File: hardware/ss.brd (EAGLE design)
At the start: 65 x 56 mm, 86 parts, among them IC1 DS3231, Q1 BSS138, Q3 si2305cd, Q4 si2305cd, Q5 8MHz, Q6 si2305cd, T1 BC846, T2 BC846, U1 SPX5205 3v3, U17 AVR_SPI_PRG_6PTH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

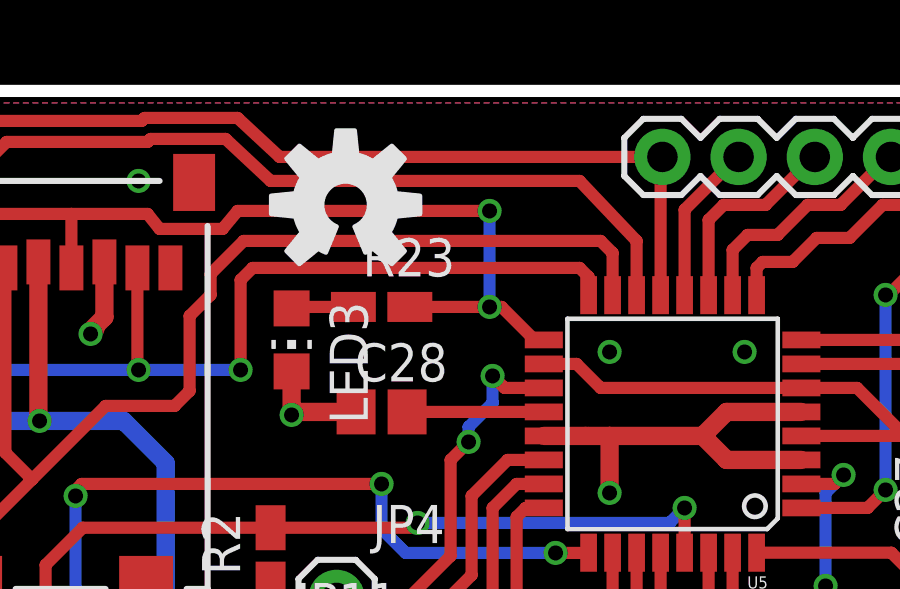
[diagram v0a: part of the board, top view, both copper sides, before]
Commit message: d9 needs external weak pullup during programming
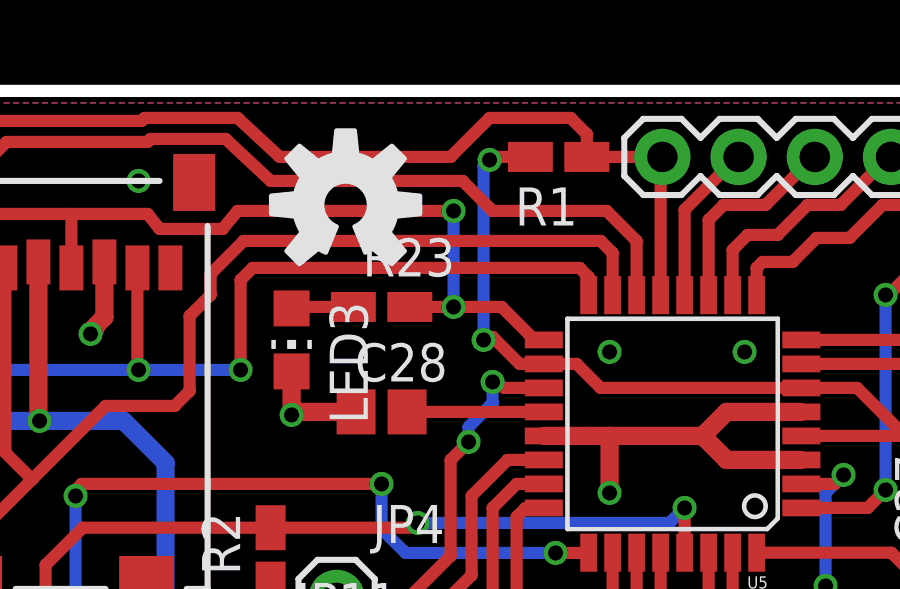
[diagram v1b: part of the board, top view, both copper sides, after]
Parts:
- added R1: 100K, rcl:R0805W
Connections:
- net +3V3: now also R1.2
- net D9: now also R1.1
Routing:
- net +3V3: track 173.7 -> 183.6 mm, vias 9 -> 11
- net D9: track 46.5 -> 48.0 mm
- net SCK: track 48.0 -> 46.8 mm
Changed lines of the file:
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@@
 <element name="R18" library="rcl" package="R0805W" value="100k" x="15.2" y="25.6" rot="R180"/>
 <element name="SJ2" library="jumper" package="SJ" value="J2" x="18.3" y="28.9" rot="R270"/>
+<element name="R1" library="rcl" package="R0805W" value="100K" x="38.1" y="53.8" rot="R180"/>
 </elements>
 <signals>
@@
 <wire x1="55.4" y1="42.7" x2="55.6" y2="42.9" width="0.6096" layer="1"/>
 <wire x1="55.6" y1="42.9" x2="57.9" y2="42.9" width="0.6096" layer="1"/>
+<contactref element="R1" pad="2"/>
+<wire x1="35.6" y1="47.7" x2="35.9" y2="47.8" width="0.4064" layer="1"/>
+<wire x1="35.9" y1="53.8" x2="35.8" y2="53.7" width="0.4064" layer="1"/>
+<wire x1="37.16" y1="53.8" x2="35.9" y2="53.8" width="0.4064" layer="1"/>
+<via x="35.6" y="47.7" extent="1-16" drill="0.5"/>
+<via x="35.8" y="53.7" extent="1-16" drill="0.5"/>
+<wire x1="35.9" y1="47.8" x2="36.8" y2="46.9" width="0.4064" layer="1"/>
+<wire x1="36.8" y1="46.9" x2="37.6074" y2="46.9" width="0.4064" layer="1"/>
+<wire x1="35.8" y1="53.7" x2="35.6" y2="53.5" width="0.4064" layer="16"/>
+<wire x1="35.6" y1="53.5" x2="35.6" y2="47.7" width="0.4064" layer="16"/>
 </signal>
 <signal name="+5V">
@@
 <wire x1="6.6" y1="45.105" x2="6.595" y2="45.1" width="0.4064" layer="1"/>
 <wire x1="37.6074" y1="47.7" x2="37.3" y2="47.7" width="0.4064" layer="1"/>
-<wire x1="35.8" y1="48.8" x2="35.8" y2="52" width="0.4064" layer="16"/>
-<via x="35.8" y="48.8" extent="1-16" drill="0.5"/>
-<via x="35.8" y="52" extent="1-16" drill="0.5"/>
+<wire x1="34.6" y1="48.8" x2="34.6" y2="52" width="0.4064" layer="16"/>
+<via x="34.6" y="48.8" extent="1-16" drill="0.5"/>
+<via x="34.6" y="52" extent="1-16" drill="0.5"/>
 <wire x1="21.86" y1="51.9" x2="21.86" y2="50.1" width="0.4064" layer="1"/>
 <wire x1="21.86" y1="51.9" x2="15.3" y2="51.9" width="0.4064" layer="1"/>
@@
 <wire x1="6.6" y1="45.105" x2="6.6" y2="41.96" width="0.6096" layer="1"/>
 <wire x1="6.6" y1="41.96" x2="6.66" y2="41.9" width="0.6096" layer="1"/>
-<wire x1="33.14" y1="48.8" x2="35.8" y2="48.8" width="0.4064" layer="1"/>
+<wire x1="33.14" y1="48.8" x2="34.6" y2="48.8" width="0.4064" layer="1"/>
 <wire x1="21.86" y1="51.9" x2="24.4" y2="51.9" width="0.4064" layer="1"/>
 <wire x1="24.4" y1="51.9" x2="24.8" y2="51.4" width="0.4064" layer="1"/>
 <wire x1="24.8" y1="51.4" x2="26.9" y2="51.4" width="0.4064" layer="1"/>
 <wire x1="26.9" y1="51.4" x2="27.4" y2="52" width="0.4064" layer="1"/>
-<wire x1="27.4" y1="52" x2="35.8" y2="52" width="0.4064" layer="1"/>
+<wire x1="27.4" y1="52" x2="34.6" y2="52" width="0.4064" layer="1"/>
 <wire x1="37.3" y1="47.7" x2="36.2" y2="48.8" width="0.4064" layer="1"/>
-<wire x1="36.2" y1="48.8" x2="35.8" y2="48.8" width="0.4064" layer="1"/>
+<wire x1="36.2" y1="48.8" x2="34.6" y2="48.8" width="0.4064" layer="1"/>
 </signal>
 <signal name="MISO">
@@
 <contactref element="U5" pad="14"/>
 <wire x1="40.7" y1="49.1926" x2="40.7" y2="51" width="0.4064" layer="1"/>
-<wire x1="40.7" y1="51" x2="38.8" y2="53" width="0.4064" layer="1"/>
-<wire x1="38.8" y1="53" x2="28.5" y2="53" width="0.4064" layer="1"/>
+<wire x1="34.9" y1="53" x2="28.5" y2="53" width="0.4064" layer="1"/>
 <wire x1="18.6" y1="48.2" x2="18.6" y2="48.4" width="0.4064" layer="1"/>
 <wire x1="18.6" y1="53" x2="18.6" y2="48.2" width="0.4064" layer="16"/>
@@
 <wire x1="19.7" y1="54.3" x2="18.6" y2="53.2" width="0.4064" layer="1"/>
 <wire x1="18.6" y1="53.2" x2="18.6" y2="53" width="0.4064" layer="1"/>
+<wire x1="34.9" y1="53" x2="35.9" y2="52" width="0.4064" layer="1"/>
+<wire x1="35.9" y1="52" x2="39.7" y2="52" width="0.4064" layer="1"/>
+<wire x1="39.7" y1="52" x2="40.7" y2="51" width="0.4064" layer="1"/>
 </signal>
 <signal name="N$22">
@@
 <wire x1="41.5" y1="49.1926" x2="41.5" y2="53.8" width="0.4064" layer="1"/>
 <wire x1="41.5" y1="53.8" x2="41.56" y2="53.8" width="0.4064" layer="1"/>
-<wire x1="28.8" y1="53.8" x2="41.56" y2="53.8" width="0.4064" layer="1"/>
 <wire x1="28.8" y1="53.8" x2="27.4" y2="55.1" width="0.4064" layer="1"/>
 <wire x1="27.4" y1="55.1" x2="24.3" y2="55.1" width="0.4064" layer="1"/>
 <wire x1="24.3" y1="55.1" x2="24.2" y2="55" width="0.4064" layer="1"/>
 <wire x1="24.2" y1="55" x2="19.1" y2="55" width="0.4064" layer="1"/>
+<contactref element="R1" pad="1"/>
+<wire x1="39.04" y1="53.8" x2="41.56" y2="53.8" width="0.4064" layer="1"/>
+<wire x1="39.04" y1="53.8" x2="39.04" y2="54.56" width="0.4064" layer="1"/>
+<wire x1="39.04" y1="54.56" x2="38.5" y2="55.1" width="0.4064" layer="1"/>
+<wire x1="38.5" y1="55.1" x2="35.8" y2="55.1" width="0.4064" layer="1"/>
+<wire x1="35.8" y1="55.1" x2="34.5" y2="53.8" width="0.4064" layer="1"/>
+<wire x1="34.5" y1="53.8" x2="28.8" y2="53.8" width="0.4064" layer="1"/>
 </signal>
 <signal name="SDA">
@@
 <contactref element="U5" pad="19"/>
 <via x="35.1" y="44.3" extent="1-16" drill="0.5"/>
-<via x="35.9" y="46.5" extent="1-16" drill="0.5"/>
+<via x="35.9" y="46.3" extent="1-16" drill="0.5"/>
 <wire x1="35.1" y1="44.8" x2="35.1" y2="44.3" width="0.4064" layer="16"/>
 <wire x1="37.6074" y1="46.1" x2="36.3" y2="46.1" width="0.4064" layer="1"/>
 <wire x1="35.1" y1="44.3" x2="34.5" y2="43.7" width="0.4064" layer="1"/>
-<wire x1="36.3" y1="46.1" x2="35.9" y2="46.5" width="0.4064" layer="1"/>
-<wire x1="35.9" y1="46.5" x2="35.9" y2="45.6" width="0.4064" layer="16"/>
+<wire x1="36.3" y1="46.1" x2="35.9" y2="46.3" width="0.4064" layer="1"/>
+<wire x1="35.9" y1="46.3" x2="35.9" y2="45.6" width="0.4064" layer="16"/>
 <wire x1="35.9" y1="45.6" x2="35.1" y2="44.8" width="0.4064" layer="16"/>
 <contactref element="JP4" pad="1"/>

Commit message: thermocouple t- must be grounded
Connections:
- removed net N$30: JP9.2, U$3.2
- net GND: now also JP9.2, U$3.2
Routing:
- net GND: track 114.2 -> 117.7 mm
- net N$30: track 3.49 -> 0.00 mm
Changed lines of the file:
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@@
 <via x="34.7" y="14.6" extent="1-16" drill="0.5"/>
 <wire x1="49.5" y1="28.1999" x2="49.5" y2="26.4" width="0.6096" layer="1"/>
+<contactref element="U$3" pad="2"/>
+<contactref element="JP9" pad="2"/>
+<wire x1="9.135" y1="50.3" x2="9.135" y2="52.595" width="0.6096" layer="1"/>
+<wire x1="9.135" y1="52.595" x2="9.84" y2="53.3" width="0.6096" layer="1"/>
+<wire x1="9.84" y1="53.3" x2="10.04" y2="53.3" width="0.6096" layer="1"/>
 </signal>
 <signal name="VIN">
@@
 <wire x1="7.5" y1="53.335" x2="7.5" y2="53.3" width="0.4064" layer="1"/>
 </signal>
-<signal name="N$30">
-<contactref element="U$3" pad="2"/>
-<contactref element="JP9" pad="2"/>
-<wire x1="9.135" y1="50.3" x2="9.135" y2="52.595" width="0.6096" layer="1"/>
-<wire x1="9.135" y1="52.595" x2="9.84" y2="53.3" width="0.6096" layer="1"/>
-<wire x1="9.84" y1="53.3" x2="10.04" y2="53.3" width="0.6096" layer="1"/>
-</signal>
 <signal name="A6">

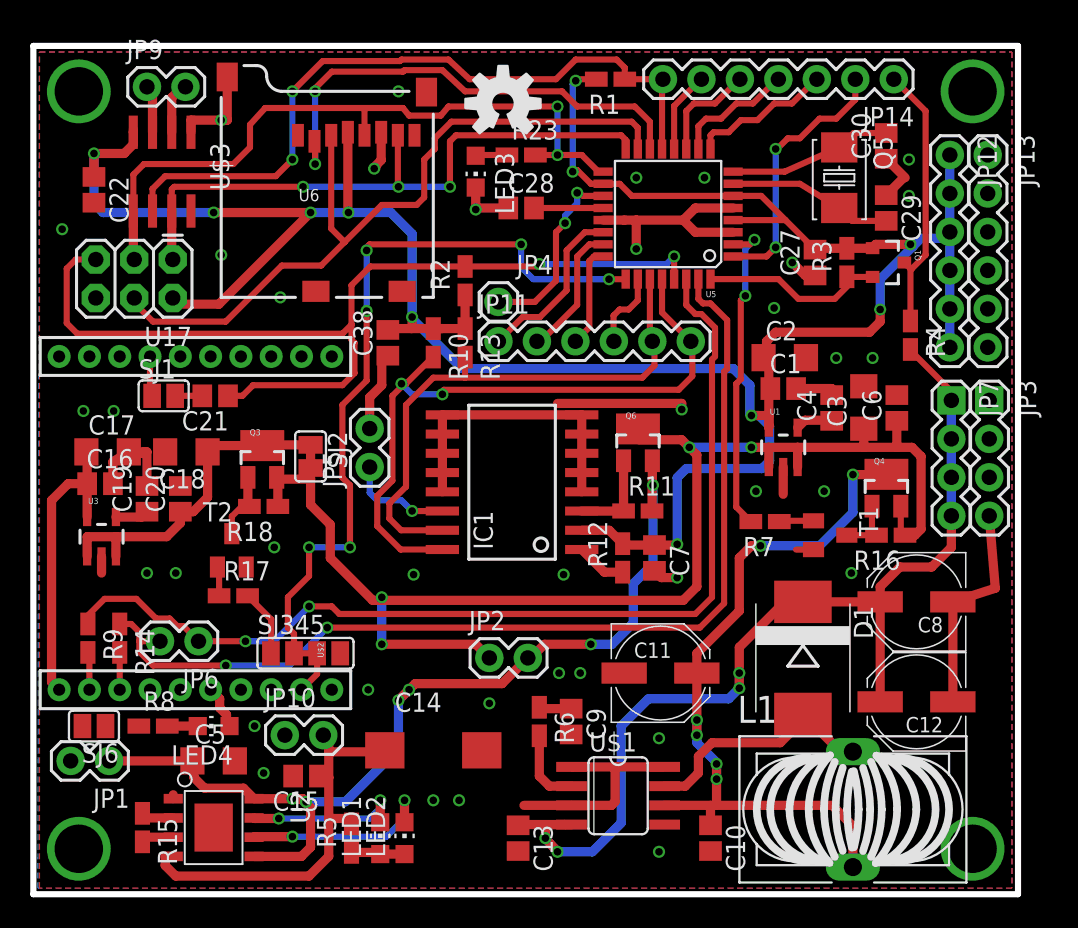
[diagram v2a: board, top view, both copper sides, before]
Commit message: move power socket
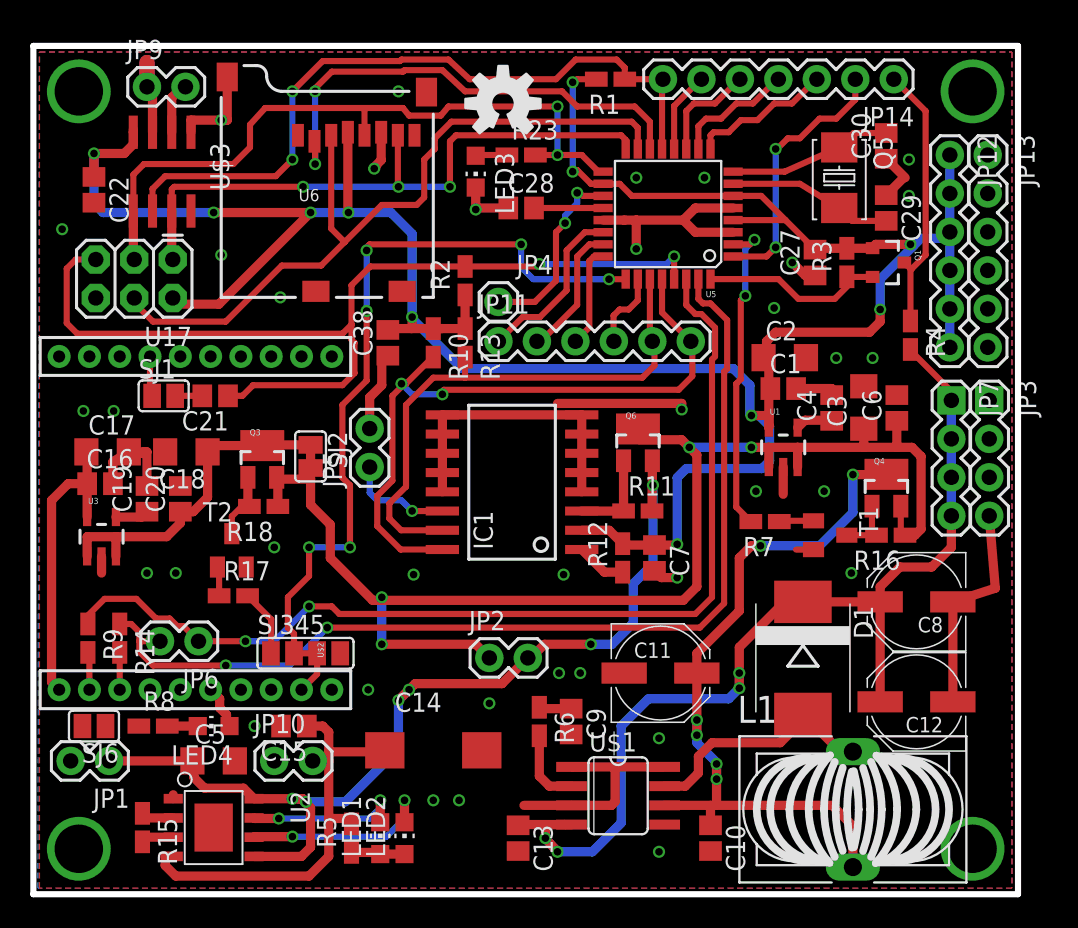
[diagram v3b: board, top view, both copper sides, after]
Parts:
- moved C15 3.40 mm to (17.2, 11.1)
- moved JP10 1.84 mm to (15.9, 8.80)
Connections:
- net N$29 renamed T+
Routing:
- net T+: track 3.44 -> 6.74 mm
- net N$12: track 27.0 -> 29.0 mm
- net GND: vias 42 -> 41
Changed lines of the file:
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@@
 <element name="C19" library="rcl" package="C0805" value="1uF" x="7.5" y="26.1" rot="R90"/>
 <element name="C20" library="rcl" package="C0805" value="100nF" x="9.7" y="26.1" rot="R90"/>
-<element name="C15" library="rcl" package="C0805" value="100nF" x="18" y="7.8" rot="R180"/>
+<element name="C15" library="rcl" package="C0805" value="100nF" x="17.2" y="11.1" rot="R180"/>
 <element name="Q4" library="Simplex-DiscreteSemi" package="SOT23-3_POWER" value="si2305cd" x="56.3" y="27"/>
 <element name="U5" library="SparkFun" package="TQFP32-08" value="ATMEGA328" x="41.9" y="44.9" rot="R180"/>
@@
 <element name="JP4" library="SparkFun-Connectors" package="1X01" value="a6" x="30.7" y="39.1"/>
 <element name="JP14" library="SparkFun-Connectors" package="1X07" value="digital" x="56.8" y="53.8" rot="R180"/>
-<element name="JP10" library="SparkFun" package="1X02" value="power" x="16.6" y="10.5"/>
+<element name="JP10" library="SparkFun" package="1X02" value="power" x="15.9" y="8.8"/>
 <element name="SJ1" library="jumper" package="SJ" value="J1" x="8.6" y="32.9"/>
 <element name="SJ6" library="jumper" package="SJ" value="J6" x="4" y="11.1" rot="R180"/>
@@
 <via x="12.4" y="42.2" extent="1-16" drill="0.5"/>
 <via x="16.3" y="39.4" extent="1-16" drill="0.5"/>
-<via x="15.2" y="8" extent="1-16" drill="0.5"/>
 <wire x1="9.233" y1="6.305" x2="9.233" y2="6.567" width="0.6096" layer="1"/>
 <via x="14.6" y="11.1" extent="1-16" drill="0.5"/>
@@
 <wire x1="9.4" y1="1.2" x2="18.2" y2="1.2" width="0.6096" layer="1"/>
 <wire x1="23.2" y1="9.5" x2="23.1" y2="9.4" width="0.6096" layer="1"/>
-<wire x1="19.5" y1="5" x2="19.5" y2="7.7" width="0.6096" layer="1"/>
-<wire x1="19.5" y1="7.7" x2="19.5" y2="9.4" width="0.6096" layer="1"/>
-<wire x1="19.5" y1="9.4" x2="19.5" y2="9.9" width="0.6096" layer="1"/>
-<wire x1="19.5" y1="9.9" x2="19.14" y2="10.26" width="0.6096" layer="1"/>
-<wire x1="19.14" y1="10.26" x2="19.14" y2="10.5" width="0.6096" layer="1"/>
+<wire x1="19.5" y1="5" x2="19.5" y2="8.8" width="0.6096" layer="1"/>
+<wire x1="19.5" y1="8.8" x2="19.5" y2="9.4" width="0.6096" layer="1"/>
 <wire x1="23.1" y1="9.4" x2="19.5" y2="9.4" width="0.6096" layer="1"/>
-<wire x1="18.85" y1="7.8" x2="18.95" y2="7.7" width="0.6096" layer="1"/>
-<wire x1="18.95" y1="7.7" x2="19.5" y2="7.7" width="0.6096" layer="1"/>
+<wire x1="19.5" y1="9.4" x2="19.5" y2="10.7" width="0.6096" layer="1"/>
+<wire x1="19.5" y1="10.7" x2="19.1" y2="11.1" width="0.6096" layer="1"/>
+<wire x1="19.1" y1="11.1" x2="18.05" y2="11.1" width="0.6096" layer="1"/>
+<wire x1="18.44" y1="8.8" x2="19.5" y2="8.8" width="0.6096" layer="1"/>
 </signal>
 <signal name="N$14">
@@
 <contactref element="R1" pad="2"/>
 <wire x1="35.6" y1="47.7" x2="35.9" y2="47.8" width="0.4064" layer="1"/>
-<wire x1="35.9" y1="53.8" x2="35.8" y2="53.7" width="0.4064" layer="1"/>
+<wire x1="35.9" y1="53.8" x2="35.6" y2="53.6" width="0.4064" layer="1"/>
 <wire x1="37.16" y1="53.8" x2="35.9" y2="53.8" width="0.4064" layer="1"/>
 <via x="35.6" y="47.7" extent="1-16" drill="0.5"/>
-<via x="35.8" y="53.7" extent="1-16" drill="0.5"/>
+<via x="35.6" y="53.6" extent="1-16" drill="0.5"/>
 <wire x1="35.9" y1="47.8" x2="36.8" y2="46.9" width="0.4064" layer="1"/>
 <wire x1="36.8" y1="46.9" x2="37.6074" y2="46.9" width="0.4064" layer="1"/>
-<wire x1="35.8" y1="53.7" x2="35.6" y2="53.5" width="0.4064" layer="16"/>
-<wire x1="35.6" y1="53.5" x2="35.6" y2="47.7" width="0.4064" layer="16"/>
+<wire x1="35.6" y1="53.6" x2="35.6" y2="47.7" width="0.4064" layer="16"/>
 </signal>
 <signal name="+5V">
@@
 <wire x1="20.9" y1="22.9" x2="20.9" y2="27" width="0.4064" layer="1"/>
 </signal>
-<signal name="N$29">
+<signal name="T+">
 <contactref element="U$3" pad="3"/>
 <contactref element="JP9" pad="1"/>
@@
 <wire x1="7.865" y1="53.335" x2="7.5" y2="53.335" width="0.4064" layer="1"/>
 <wire x1="7.5" y1="53.335" x2="7.5" y2="53.3" width="0.4064" layer="1"/>
+<wire x1="7.5" y1="53.3" x2="7.6" y2="53.3" width="0.6096" layer="1"/>
+<wire x1="7.5" y1="54.9" x2="7.5" y2="53.3" width="1.016" layer="16"/>
+<wire x1="7.5" y1="53.3" x2="7.5" y2="54.9" width="1.016" layer="1"/>
 </signal>
 <signal name="A6">
